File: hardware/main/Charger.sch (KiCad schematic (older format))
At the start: 68 parts, among them K1 K100A, K802 SANYOU_SRD_Form_C, Q801 BCV27, Q802 Q_NPN_BEC, Q803 BCV27, U2 K100B

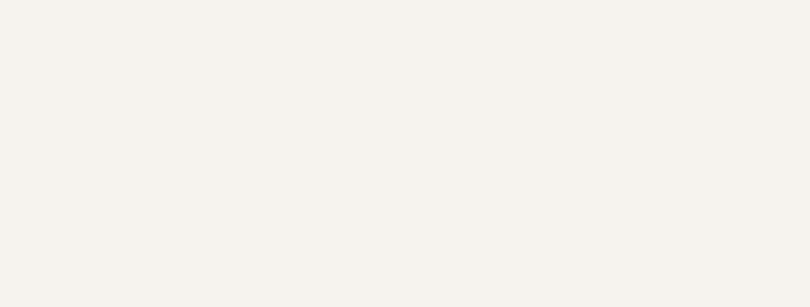
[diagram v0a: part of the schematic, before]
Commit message: Ampop layout not finished
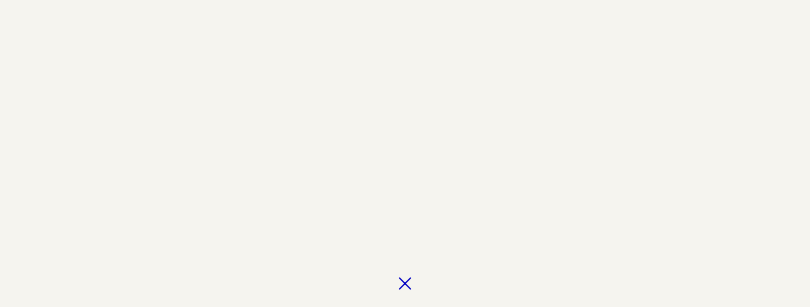
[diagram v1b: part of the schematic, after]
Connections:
- no-connect marks 1 -> 2
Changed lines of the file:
@@
 	0    -1   -1   0
 $EndComp
+NoConn ~ 6300 11300
 $EndSCHEMATC

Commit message: Layout retrabalhado. Não finalizado.
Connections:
- net +CAP: now also JP801.1; no longer JP802.1
- net U_BAT+: now also JP802.1; no longer JP801.1
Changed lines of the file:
@@
 EESchema Schematic File Version 4
 LIBS:main-cache
-EELAYER 26 0
+EELAYER 29 0
 EELAYER END
 $Descr A3 16535 11693
@@
 Wire Wire Line
 	6400 8400 7100 8400
+Text Label 6600 8050 0    39   ~ 0
++CAP
 Text Label 6600 8300 0    39   ~ 0
-+CAP
-Text Label 6600 8050 0    39   ~ 0
 U_BAT+
 $Comp
@@
 Wire Wire Line
 	7950 8600 7950 8450
+Text HLabel 8200 8350 2    50   Output ~ 0
+sig_bat+
 Text HLabel 8200 8100 2    50   Output ~ 0
-sig_bat+
-Text HLabel 8200 8350 2    50   Output ~ 0
 sig_cap+
 $Comp

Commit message: First version PCB
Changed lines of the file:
@@
 $EndComp
 NoConn ~ 6300 11300
+$Comp
+L Graphic:Logo_Open_Hardware_Small #LOGO2
+U 1 1 5CC3B73E
+P 10700 8800
+F 0 "#LOGO2" H 10700 9075 50  0001 C CNN
+F 1 "Logo_Open_Hardware_Small" H 10700 8575 50  0001 C CNN
+F 2 "Symbol:OSHW-Logo2_9.8x8mm_Copper" H 10700 8800 50  0001 C CNN
+F 3 "~" H 10700 8800 50  0001 C CNN
+	1    10700 8800
+	1    0    0    -1
+$EndComp
+$Comp
+L Graphic:Logo_Open_Hardware_Small #LOGO1
+U 1 1 5CC3C3FD
+P 10700 8150
+F 0 "#LOGO1" H 10700 8425 50  0001 C CNN
+F 1 "Zenite" H 10700 7925 50  0001 C CNN
+F 2 "KicadZeniteSolarLibrary18:zenite" H 10700 8150 50  0001 C CNN
+F 3 "~" H 10700 8150 50  0001 C CNN
+	1    10700 8150
+	1    0    0    -1
+$EndComp
 $EndSCHEMATC

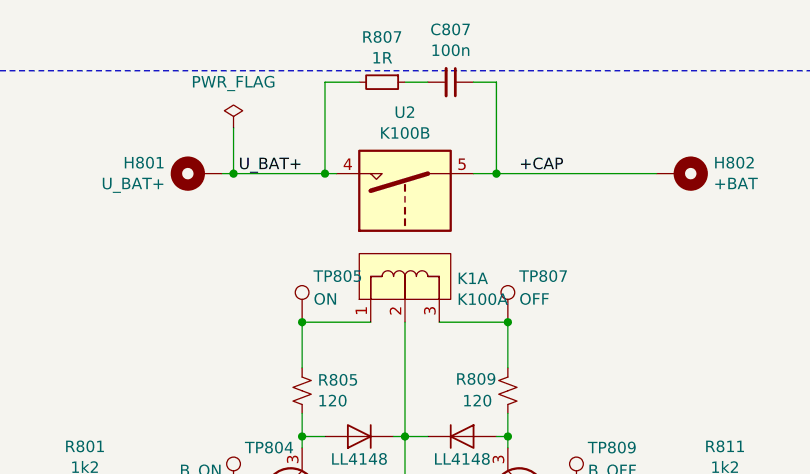
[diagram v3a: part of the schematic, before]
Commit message: Connector to join the modules, were centrailized Compacted Atmega PCB
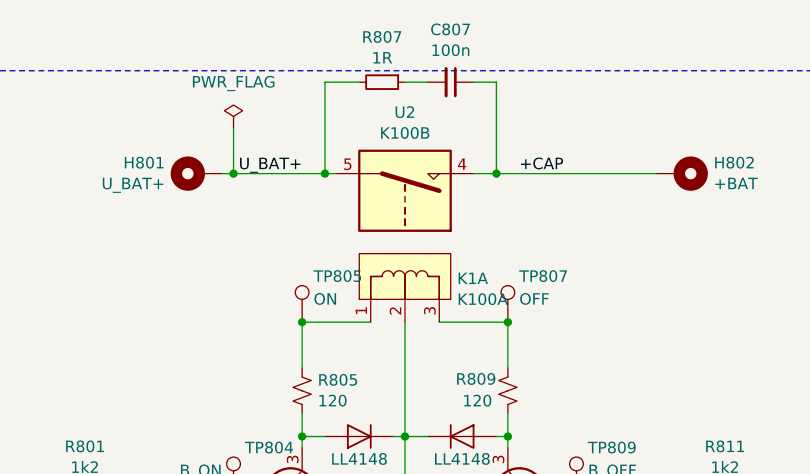
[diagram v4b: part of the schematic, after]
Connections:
- net +CAP: now also U2.4; no longer U2.5
- net U_BAT+: now also U2.5; no longer U2.4
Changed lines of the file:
@@
 EESchema Schematic File Version 4
 LIBS:main-cache
-EELAYER 29 0
+EELAYER 26 0
 EELAYER END
 $Descr A3 16535 11693
@@
 F 3 "" H 2550 1200 50  0001 C CNN
 	1    2800 1350
-	0    -1   -1   0
+	0    1    -1   0
 $EndComp
 NoConn ~ 6300 11300

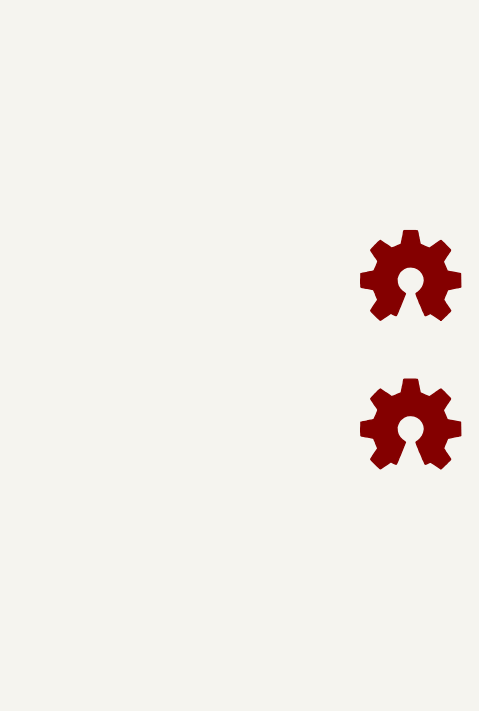
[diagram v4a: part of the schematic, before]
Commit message: Ampop gain error
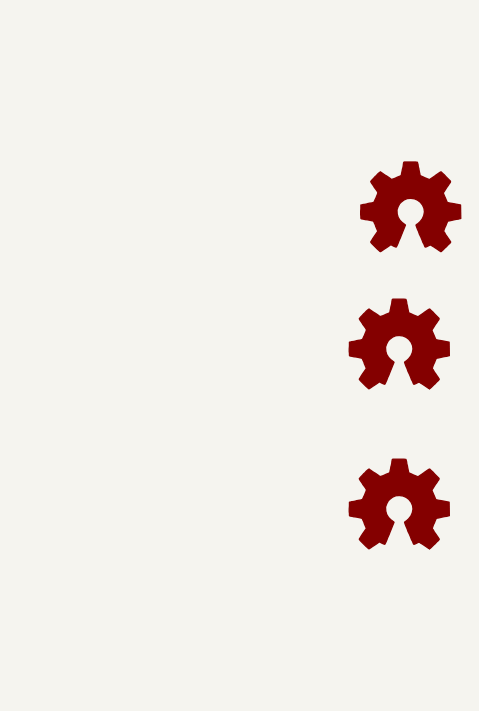
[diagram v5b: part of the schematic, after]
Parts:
- added LOGO1: Logo_Open_Hardware_Small, KicadZeniteSolarLibrary18:zenite, symbol Graphic:Logo_Open_Hardware_Small
- added LOGO2: Logo_Open_Hardware_Small, Symbol:OSHW-Logo2_9.8x8mm_Copper, symbol Graphic:Logo_Open_Hardware_Small
- added LOGO3: Logo_Open_Hardware_Small, Symbol:KiCad-Logo2_5mm_Copper, symbol Graphic:Logo_Open_Hardware_Small
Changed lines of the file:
@@
 EESchema Schematic File Version 4
 LIBS:main-cache
-EELAYER 26 0
+EELAYER 29 0
 EELAYER END
 $Descr A3 16535 11693
@@
 NoConn ~ 6300 11300
 $Comp
-L Graphic:Logo_Open_Hardware_Small #LOGO2
-U 1 1 5CC3B73E
-P 10700 8800
-F 0 "#LOGO2" H 10700 9075 50  0001 C CNN
-F 1 "Logo_Open_Hardware_Small" H 10700 8575 50  0001 C CNN
-F 2 "Symbol:OSHW-Logo2_9.8x8mm_Copper" H 10700 8800 50  0001 C CNN
-F 3 "~" H 10700 8800 50  0001 C CNN
-	1    10700 8800
-	1    0    0    -1
-$EndComp
-$Comp
-L Graphic:Logo_Open_Hardware_Small #LOGO1
-U 1 1 5CC3C3FD
-P 10700 8150
-F 0 "#LOGO1" H 10700 8425 50  0001 C CNN
-F 1 "Zenite" H 10700 7925 50  0001 C CNN
-F 2 "KicadZeniteSolarLibrary18:zenite" H 10700 8150 50  0001 C CNN
-F 3 "~" H 10700 8150 50  0001 C CNN
-	1    10700 8150
-	1    0    0    -1
-$EndComp
+L Graphic:Logo_Open_Hardware_Small LOGO2
+U 1 1 5CC0B817
+P 10650 9150
+F 0 "LOGO2" H 10650 9425 50  0001 C CNN
+F 1 "Logo_Open_Hardware_Small" H 10650 8925 50  0001 C CNN
+F 2 "Symbol:OSHW-Logo2_9.8x8mm_Copper" H 10650 9150 50  0001 C CNN
+F 3 "~" H 10650 9150 50  0001 C CNN
+	1    10650 9150
+	1    0    0    -1
+$EndComp
+$Comp
+L Graphic:Logo_Open_Hardware_Small LOGO1
+U 1 1 5CC0BA8B
+P 10650 8450
+F 0 "LOGO1" H 10650 8725 50  0001 C CNN
+F 1 "Logo_Open_Hardware_Small" H 10650 8225 50  0001 C CNN
+F 2 "KicadZeniteSolarLibrary18:zenite" H 10650 8450 50  0001 C CNN
+F 3 "~" H 10650 8450 50  0001 C CNN
+	1    10650 8450
+	1    0    0    -1
+$EndComp
+$Comp
+L Graphic:Logo_Open_Hardware_Small LOGO3
+U 1 1 5CC0BCBA
+P 10700 7850
+F 0 "LOGO3" H 10700 8125 50  0001 C CNN
+F 1 "Logo_Open_Hardware_Small" H 10700 7625 50  0001 C CNN
+F 2 "Symbol:KiCad-Logo2_5mm_Copper" H 10700 7850 50  0001 C CNN
+F 3 "~" H 10700 7850 50  0001 C CNN
+	1    10700 7850
+	1    0    0    -1
+$EndComp
